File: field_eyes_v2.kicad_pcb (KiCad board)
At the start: 2 copper layers, 96 x 72 mm, 156 parts, among them J101 SOLAR 6V, J201 PROG, J202 OLED, J203 DHT22, J301 U.FL LTE, J302 SIM holder (TE 2199337-5), J303 MODEM USB (DNP), J401 SMT100 (V+ GND A B), J402 7-in-1 NPK (V+ GND A B), J403 VALVE coil, Q101 AO3401A, Q102 AO3401A, Q103 2N7002, Q104 FS8205, Q105 AO3401A, Q106 2N7002, Q107 AO3401A, Q108 2N7002, Q201 MMBT3904, Q202 MMBT3904, Q301 MMBT3904, Q302 MMBT3904, Q303 MMBT3904, Q304 MMBT3904, Q305 MMBT3904, Q306 MMBT3904, Q401 MMBT3904, Q402 MMBT3904, SW201 RESET, SW202 BOOT, U101 CN3791, U102 DW01A, U103 XC6220B331MR, U104 MT3608, U201 ESP32-WROOM-32D, U301 A7672S, U302 SMF05C, U401 SP3485EN, U402 SP3485EN, U403 MX1508, U404 L78L09

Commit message: repositioned ccomponents
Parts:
- removed J201: PROG, Connector_PinHeader_2.54mm:PinHeader_1x06_P2.54mm_Vertical
- removed J202: OLED, Connector_PinHeader_2.54mm:PinHeader_1x04_P2.54mm_Vertical
- removed J203: DHT22, Connector_PinHeader_2.54mm:PinHeader_1x03_P2.54mm_Vertical
- removed J401: SMT100 (V+ GND A B), TerminalBlock_Phoenix:TerminalBlock_Phoenix_PT-1,5-4-3.5-H_1x04_P3.50mm_Horizontal
- removed J402: 7-in-1 NPK (V+ GND A B), TerminalBlock_Phoenix:TerminalBlock_Phoenix_PT-1,5-4-3.5-H_1x04_P3.50mm_Horizontal
- added C313: 33pF, Capacitor_SMD:C_0402_1005Metric, F.Cu at (174.8, 72.0)
- added C408: 330nF 25V, Capacitor_SMD:C_0603_1608Metric, F.Cu at (125.3, 84.6)
- added C409: 1uF, Capacitor_SMD:C_0603_1608Metric, F.Cu at (113.5, 80.7)
- added J304: U.FL GPS, Connector_Coaxial:U.FL_Hirose_U.FL-R-SMT-1_Vertical, F.Cu at (173.8, 66.5)
- added L301: 56nH, Inductor_SMD:L_0805_2012Metric, F.Cu at (171.6, 71.9)
- added R318: 0R, Resistor_SMD:R_0603_1608Metric, F.Cu at (169.3, 71.9)
- added R319: 10k, Resistor_SMD:R_0603_1608Metric, F.Cu at (207.2, 71.7)
- added R320: 1k, Resistor_SMD:R_0603_1608Metric, F.Cu at (195.7, 101.3)
- added R321: 1k, Resistor_SMD:R_0603_1608Metric, F.Cu at (198.4, 101.3)
- added R423: 3.3k, Resistor_SMD:R_0603_1608Metric, F.Cu at (128.3, 99.4)
- added R424: 6.8k, Resistor_SMD:R_0603_1608Metric, F.Cu at (131.5, 94.9)
- added R425: 3.3k, Resistor_SMD:R_0603_1608Metric, F.Cu at (127.9, 103.6)
- added R426: 6.8k, Resistor_SMD:R_0603_1608Metric, F.Cu at (139.2, 93.7)
- added SV1: PROG (as old SV1), field_eyes:MA03-2, F.Cu at (164.7, 65.4)
- added U405: L78L05, Package_TO_SOT_SMD:SOT-89-3, F.Cu at (122.6, 80.8)
- added X1: 7-in-1 NPK (A B 12V GND), field_eyes:JST_XH_04_LongPad, F.Cu at (159.5, 116.4)
- added X2: SMT100 (A B 12V GND), field_eyes:JST_XH_04_LongPad, F.Cu at (145.3, 116.5)
- added X3: OLED (3V3 GND SDA SCL), field_eyes:JST_XH_04_LongPad, F.Cu at (169.4, 83.1)
- added X4: DHT22 (NC 3V3 DATA GND), field_eyes:JST_XH_04_LongPad, F.Cu at (173.7, 116.4)
- U401, U402: value SP3485EN -> MAX485ESA+T
- moved R313 93.7 mm to (208.3, 75.2)
- moved D302 93.2 mm to (210.2, 91.2), turned to 180 degrees
- moved R311 88.9 mm to (211.6, 96.1)
- moved Q306 87.7 mm to (207.2, 94.5), turned to 90 degrees
- moved R312 84.6 mm to (211.1, 93.9)
- moved R310 80.7 mm to (198.2, 65.2)
- moved R304 79.1 mm to (193.7, 63.0)
- moved C309 78.8 mm to (199.7, 69.4)
- moved R207 78.5 mm to (163.8, 80.7)
- moved R307 77.5 mm to (196.3, 71.5)
- moved R205 76.2 mm to (163.1, 82.6)
- moved R301 75.7 mm to (194.4, 67.0)
- moved Q301 75.4 mm to (190.4, 66.2)
- moved Q303 73.7 mm to (192.1, 70.0)
- moved J303 73.2 mm to (205.6, 111.1)
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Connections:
- C401 pad 1: +3V3_SW -> +5V_SENS
- C402 pad 1: +3V3_SW -> +5V_SENS
- R402 pad 1: +3V3_SW -> +5V_SENS
- R403 pad 1: +3V3_SW -> +5V_SENS
- R412 pad 1: +3V3_SW -> +5V_SENS
- R413 pad 1: +3V3_SW -> +5V_SENS
- U301 pad P$116: (no net) -> +3V3
- U301 pad P$20: (no net) -> /MK_IN_3
- U301 pad P$49: (no net) -> /U3_RXD
- U301 pad P$50: (no net) -> /U3_TXD
- U301 pad P$90: (no net) -> /GPS_ANT
- U301 pad P$95: (no net) -> /GNSS_TXD
- U301 pad P$96: (no net) -> /GNSS_RXD
- U301 pad P$97: (no net) -> /VDD_1V8
- U301 pad P$98: (no net) -> /GNSS_PWRCTL
- U301 pad P$99: (no net) -> /VDD_2V8
- U401 pad 1: SMT_RX -> /RS1_RO
- U401 pad 8: +3V3_SW -> +5V_SENS
- U402 pad 1: NPK_RX -> /RS2_RO
- U402 pad 8: +3V3_SW -> +5V_SENS
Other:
- board size 96 x 72 mm -> 128.3 x 60 mm

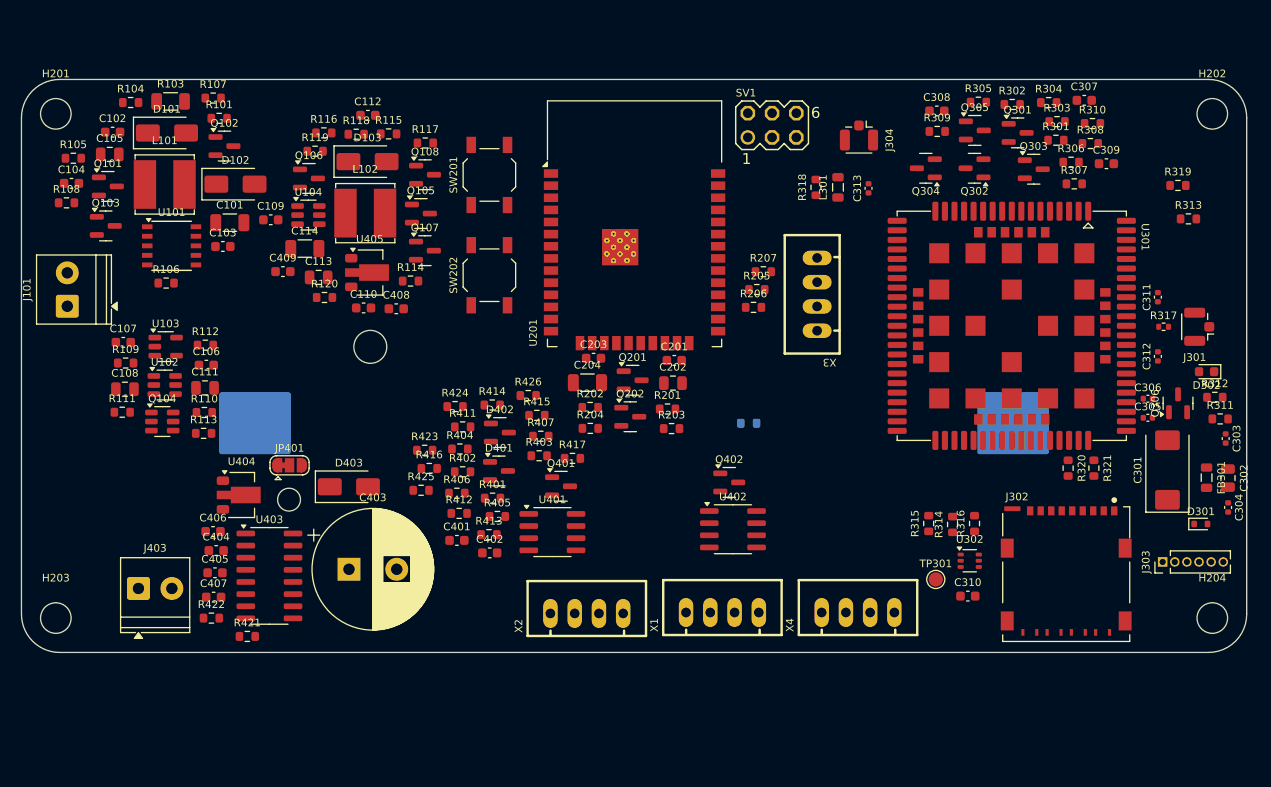
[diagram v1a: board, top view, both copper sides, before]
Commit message: removed buttons
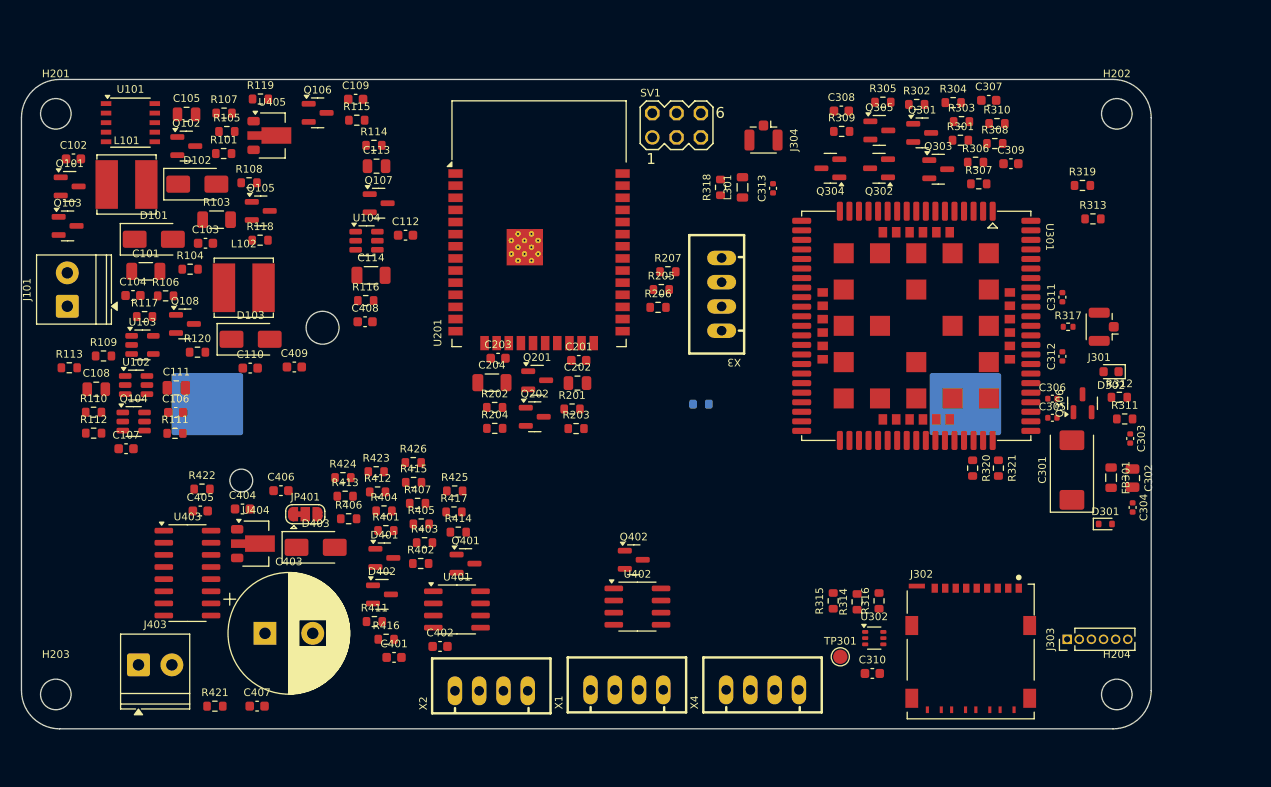
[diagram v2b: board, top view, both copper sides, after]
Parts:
- removed SW201: RESET, Button_Switch_SMD:SW_SPST_TL3342
- removed SW202: BOOT, Button_Switch_SMD:SW_SPST_TL3342
- moved R117 34.6 mm to (99.0, 85.4)
- moved Q108 29.6 mm to (103.2, 86.2)
- moved R411 22.4 mm to (123.0, 117.4)
- moved D103 22.3 mm to (110.1, 87.8)
- moved D402 21.0 mm to (123.8, 114.5)
- moved R108 19.2 mm to (109.9, 71.4)
- moved R104 18.5 mm to (103.8, 80.5)
- moved R416 18.4 mm to (124.3, 119.2)
- moved R116 18.1 mm to (122.1, 83.8)
- moved U405 17.6 mm to (112.4, 66.5)
- moved Q105 16.8 mm to (111.2, 74.4)
- moved R105 16.3 mm to (107.6, 66.1)
- moved R113 15.7 mm to (91.1, 90.8)
- moved R413 15.6 mm to (120.0, 104.2)
- moved C109 15.4 mm to (121.1, 62.7)
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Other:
- board size 128.3 x 60 mm -> 118.3 x 68 mm

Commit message: spaced components
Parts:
- moved R411 37.8 mm to (158.5, 104.2)
- moved R113 32.5 mm to (123.4, 94.6)
- moved C109 29.7 mm to (120.1, 92.3)
- moved R309 28.6 mm to (199.5, 73.6)
- moved Q107 28.0 mm to (103.6, 93.2)
- moved Q106 27.8 mm to (114.0, 91.8)
- moved R119 27.5 mm to (107.0, 89.8)
- moved R415 27.2 mm to (154.1, 106.3)
- moved C202 27.1 mm to (164.8, 110.1)
- moved R417 26.5 mm to (156.4, 114.6)
- moved R201 26.2 mm to (163.3, 112.6)
- moved R115 25.2 mm to (122.0, 90.1)
- moved R412 24.6 mm to (147.4, 98.6)
- moved C309 24.5 mm to (166.2, 62.4)
- moved R112 24.3 mm to (117.9, 95.7)
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
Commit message: routed the board
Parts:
- moved C311 9.77 mm to (195.0, 84.7)
- moved R317 9.14 mm to (196.1, 86.4)
- moved SV1 6.40 mm to (154.7, 71.8)
- moved C312 6.28 mm to (197.3, 85.6)
- moved C313 5.06 mm to (167.3, 69.8)
- moved L301 4.33 mm to (161.3, 71.1), turned to -90 degrees
- moved R318 2.84 mm to (161.3, 74.6), turned to -90 degrees
- moved R205 2.00 mm to (156.2, 78.4)
- moved R206 2.00 mm to (156.1, 80.6)
- moved R207 2.00 mm to (156.2, 76.2)
- turned J301 to 0 degrees
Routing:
- net +3V3: track 0.00 -> 335.0 mm, vias 0 -> 36
- net VSYS: track 0.00 -> 210.3 mm, vias 0 -> 11
- net GND: track 0.00 -> 182.6 mm, vias 0 -> 90
- net +3V3_SW: track 0.00 -> 135.1 mm, vias 0 -> 7
- net +12V_SENS: track 0.00 -> 128.8 mm, vias 0 -> 2
- net /BATN: track 0.00 -> 116.5 mm, vias 0 -> 5
- net +5V_SENS: track 0.00 -> 113.6 mm, vias 0 -> 12
- net /VDD_1V8: track 0.00 -> 81.1 mm, vias 0 -> 2
- net RI_WAKE: track 0.00 -> 73.7 mm, vias 0 -> 7
- net CHG_INHIBIT: track 0.00 -> 68.6 mm, vias 0 -> 3
- net BAT_V: track 0.00 -> 67.8 mm, vias 0 -> 4
- net VALVE_IN1: track 0.00 -> 67.4 mm, vias 0 -> 7
- net VALVE_IN2: track 0.00 -> 66.2 mm, vias 0 -> 5
- net /MODEM_VBAT: track 0.00 -> 63.4 mm, vias 0 -> 3
- net /SOLAR_P: track 0.00 -> 62.4 mm, vias 0 -> 2
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- added copper zone on B.Cu, net GND
- added copper zone on F.Cu, net GND
